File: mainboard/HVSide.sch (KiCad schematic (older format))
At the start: 50 parts, among them J11 CONN_2X2, J17 HV, J18 CONN_1X2, J19 CONN_1X2, J4 CONN_2X2, U10 DCDC_ISO_5V_ISO, U15 CD4082, U16 ADCMP350, U19 TCMT1103, U23 CD4072BPW, U24 LM358, U26 TCMT1103, U27 DCDC_ISO_5V, U28 MIC5365-3.3YC5, U29 Si8900, U30 MAX14878AWA+, U7 ADCMP354

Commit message: Added 64pin mcu and moved isocanspi to HV sheet
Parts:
- added C? (x3): 100nF, Capacitor_SMD:C_0603_1608Metric, symbol Device:C_Small
- added R?: 330K, Resistor_SMD:R_0603_1608Metric, symbol Device:R
- added R?: 604, Resistor_SMD:R_0603_1608Metric, symbol Device:R
- added R?: 1K4, Resistor_SMD:R_0603_1608Metric, symbol Device:R
- added R? (x2): 150, Resistor_SMD:R_0603_1608Metric, symbol Device:R
- added R?: 120, Resistor_SMD:R_0805_2012Metric, symbol Device:R
- added U?: HM2103, MainBoard:HM2103, symbol MainBoard:HM2103
- added U?: LTC6820, MainBoard:MSOP-16, symbol MainBoard:LTC6820
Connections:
- net +3V3: now also C?.1, R?.1, U?.6 (VDDs)
- net +5V: now also C?.1, U?.12 (MSTR), U?.9 (VDD)
- net GND: now also C?.1, C?.2, C?.2, R?.1, U?.1 (EN), U?.13 (SLOW), U?.14 (GND), U?.7 (POL), U?.8 (PHA)
- net ISO_CANH renamed ISO_CANH_IP
- net ISO_CANH_IP: now also J11.1 (Pin_1), R?.2, U?.3; no longer J11.2 (Pin_2)
- net ISO_CANL renamed ISO_CANL_IM
- net ISO_CANL_IM: now also J11.2 (Pin_2), R?.1, U?.1; no longer J11.1 (Pin_1)
- new net: C?.2, R?.1, R?.2
- new net CS_6820: U?.5 (~CS)
- new net IBIAS: R?.2, U?.16 (IBIAS)
- new net ICMP: R?.1, R?.2, U?.15 (ICMP)
- new net IM_LV: R?.2, U?.10 (IM), U?.6
- new net IP_LV: R?.1, U?.11 (IP), U?.4
- new net MOSI: U?.2 (MOSI)
- new net SCK: U?.4 (SCK)
- no-connect marks 6 -> 8
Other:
- note added: "ISOLATED PACK VOLTAGE ADC via UART"
- note added: "ISOLATED VOLTAGE SUPPLIES"
- note added: "PRECHARGE_STATUS = TS_exceed_60Vdc & PRECHARGE_ON\n"
- note added: "PROMINENT INDICATOR"
- note added: "choose only one between up or down circuits"
- note added: "isoCAN INTERFACE"
- note added: "isoCAN/SPI"
- note added: "isoSPI INTERFACE"
- note added: "isolation"
- note removed: "CAN_ISO"
- note removed: "ISOLATED VOLTAGE SOURCES"
- note removed: "PRECHARGE_STATUS = TS_exceed_60Vdc && PRECHARGE_ON\n"
- note removed: "PROMINENT INDICTOR"
- note removed: "UART ISOLATED PACK VOLTAGE ADC"
- moved on the sheet: C16, C17, C27, J11, J17, J18, J19, J4, R59, U10, U16, U30

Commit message: added the stm32 configuration, neaten schematic
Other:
- note added: "HV"
- note added: "LV"
- moved on the sheet: C16, C17, C26, C27, C40, C41, C43, C?, D4, J11, J17, J18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

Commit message: general changes and comments, still WIP
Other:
- note added: "Isolated power supply to power the \nHV-side elements from the BMS-side 5V"
- note added: "Prominent\nIndicator\n25mA"
- note added: "Supply from the first cell to be \nsure the prominent is powered.\nONLY CONNECT THE FIRST CELL\n BECAUSE OF BOARD CLEARANCES"
- note removed: "Prominent\nIndicator"
- moved on the sheet: C17, U10
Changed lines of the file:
@@
 Wire Wire Line
 	1050 3100 950  3100
-Text Notes 4650 1000 2    50   ~ 0
-Prominent\nIndicator
+Text Notes 4250 1000 0    50   ~ 0
+Prominent\nIndicator\n25mA
 Wire Wire Line
 	7000 4100 7250 4100
@@
 Text HLabel 8200 1100 2    50   Input ~ 0
 si890x_reset
-Text Label 1950 1300 0    50   ~ 0
+Text Label 1950 1150 0    50   ~ 0
 5V_FROM_CELL
 $Comp
 L Device:C C17
 U 1 1 5E5BFB93
-P 2350 1450
-F 0 "C17" H 2465 1496 50  0000 L CNN
-F 1 "1uF" H 2465 1405 50  0000 L CNN
-F 2 "Capacitor_SMD:C_0805_2012Metric" H 2388 1300 50  0001 C CNN
-F 3 "https://www.mouser.it/ProductDetail/AVX/12102C105KAZ2A?qs=sGAEpiMZZMs0AnBnWHyRQN7%2FAA2D2lPPDCdjTtfSValCgVFFyRxU%2FQ%3D%3D" H 2350 1450 50  0001 C CNN
-	1    2350 1450
+P 2350 1300
+F 0 "C17" H 2465 1346 50  0000 L CNN
+F 1 "1uF" H 2465 1255 50  0000 L CNN
+F 2 "Capacitor_SMD:C_0805_2012Metric" H 2388 1150 50  0001 C CNN
+F 3 "https://www.mouser.it/ProductDetail/AVX/12102C105KAZ2A?qs=sGAEpiMZZMs0AnBnWHyRQN7%2FAA2D2lPPDCdjTtfSValCgVFFyRxU%2FQ%3D%3D" H 2350 1300 50  0001 C CNN
+	1    2350 1300
 	1    0    0    -1
 $EndComp
@@
 L power:-BATT #PWR0104
 U 1 1 5E5C001A
-P 2350 1600
-F 0 "#PWR0104" H 2350 1450 50  0001 C CNN
-F 1 "-BATT" H 2350 1750 50  0000 C CNN
-F 2 "" H 2350 1600 50  0001 C CNN
-F 3 "" H 2350 1600 50  0001 C CNN
-	1    2350 1600
-	-1   0    0    1
-$EndComp
-Wire Wire Line
-	1950 1300 2350 1300
+P 2350 1450
+F 0 "#PWR0104" H 2350 1300 50  0001 C CNN
+F 1 "-BATT" H 2350 1600 50  0000 C CNN
+F 2 "" H 2350 1450 50  0001 C CNN
+F 3 "" H 2350 1450 50  0001 C CNN
+	1    2350 1450
+	-1   0    0    1
+$EndComp
+Wire Wire Line
+	1950 1150 2350 1150
 $Comp
 L Device:C C26
@@
 L MainBoard:DCDC_ISO_12V_ISO U10
 U 1 1 5E5FCD5F
-P 1500 1300
-F 0 "U10" H 1525 1565 50  0000 C CNN
-F 1 "DCDC_ISO_5V_ISO" H 1525 1474 50  0000 C CNN
-F 2 "MainBoard:DC_DC_ISO_ROExxxx" H 1500 1300 50  0001 C CNN
-F 3 "" H 1500 1300 50  0001 C CNN
-	1    1500 1300
+P 1500 1150
+F 0 "U10" H 1525 1415 50  0000 C CNN
+F 1 "DCDC_ISO_5V_ISO" H 1525 1324 50  0000 C CNN
+F 2 "MainBoard:DC_DC_ISO_ROExxxx" H 1500 1150 50  0001 C CNN
+F 3 "" H 1500 1150 50  0001 C CNN
+	1    1500 1150
 	1    0    0    -1
 $EndComp
@@
 L power:-BATT #PWR0106
 U 1 1 5E616F05
-P 1950 1450
-F 0 "#PWR0106" H 1950 1300 50  0001 C CNN
-F 1 "-BATT" H 1950 1600 50  0000 C CNN
-F 2 "" H 1950 1450 50  0001 C CNN
-F 3 "" H 1950 1450 50  0001 C CNN
-	1    1950 1450
+P 1950 1300
+F 0 "#PWR0106" H 1950 1150 50  0001 C CNN
+F 1 "-BATT" H 1950 1450 50  0000 C CNN
+F 2 "" H 1950 1300 50  0001 C CNN
+F 3 "" H 1950 1300 50  0001 C CNN
+	1    1950 1300
 	1    0    0    1
 $EndComp
@@
 Text Notes 5800 1300 0    50   ~ 0
 IMD_TS+
-Text Notes 1050 950  0    50   ~ 0
+Text Notes 1900 550  0    50   ~ 0
 EXT_POWER&PROMIMENT
 Text Notes 4650 5200 0    50   ~ 0
@@
 Text Label 2300 800  2    50   ~ 0
 EXT_5V
-Text Label 650  1450 0    50   ~ 0
+Text Label 650  1300 0    50   ~ 0
 EXT_GND
 Wire Wire Line
-	1100 1300 650  1300
-Text Label 650  1300 0    50   ~ 0
+	1100 1150 650  1150
+Text Label 650  1150 0    50   ~ 0
 EXT_5V
 Wire Wire Line
-	650  1450 1100 1450
+	650  1300 1100 1300
 Wire Notes Line
 	4150 650  4150 1200
@@
 Text Notes 4050 7750 1    50   Italic 0
 LV
+Text Notes 550  1750 0    50   ~ 0
+Supply from the first cell to be \nsure the prominent is powered.\nONLY CONNECT THE FIRST CELL\n BECAUSE OF BOARD CLEARANCES
+Text Notes 6950 3300 0    50   ~ 0
+Isolated power supply to power the \nHV-side elements from the BMS-side 5V
 $EndSCHEMATC

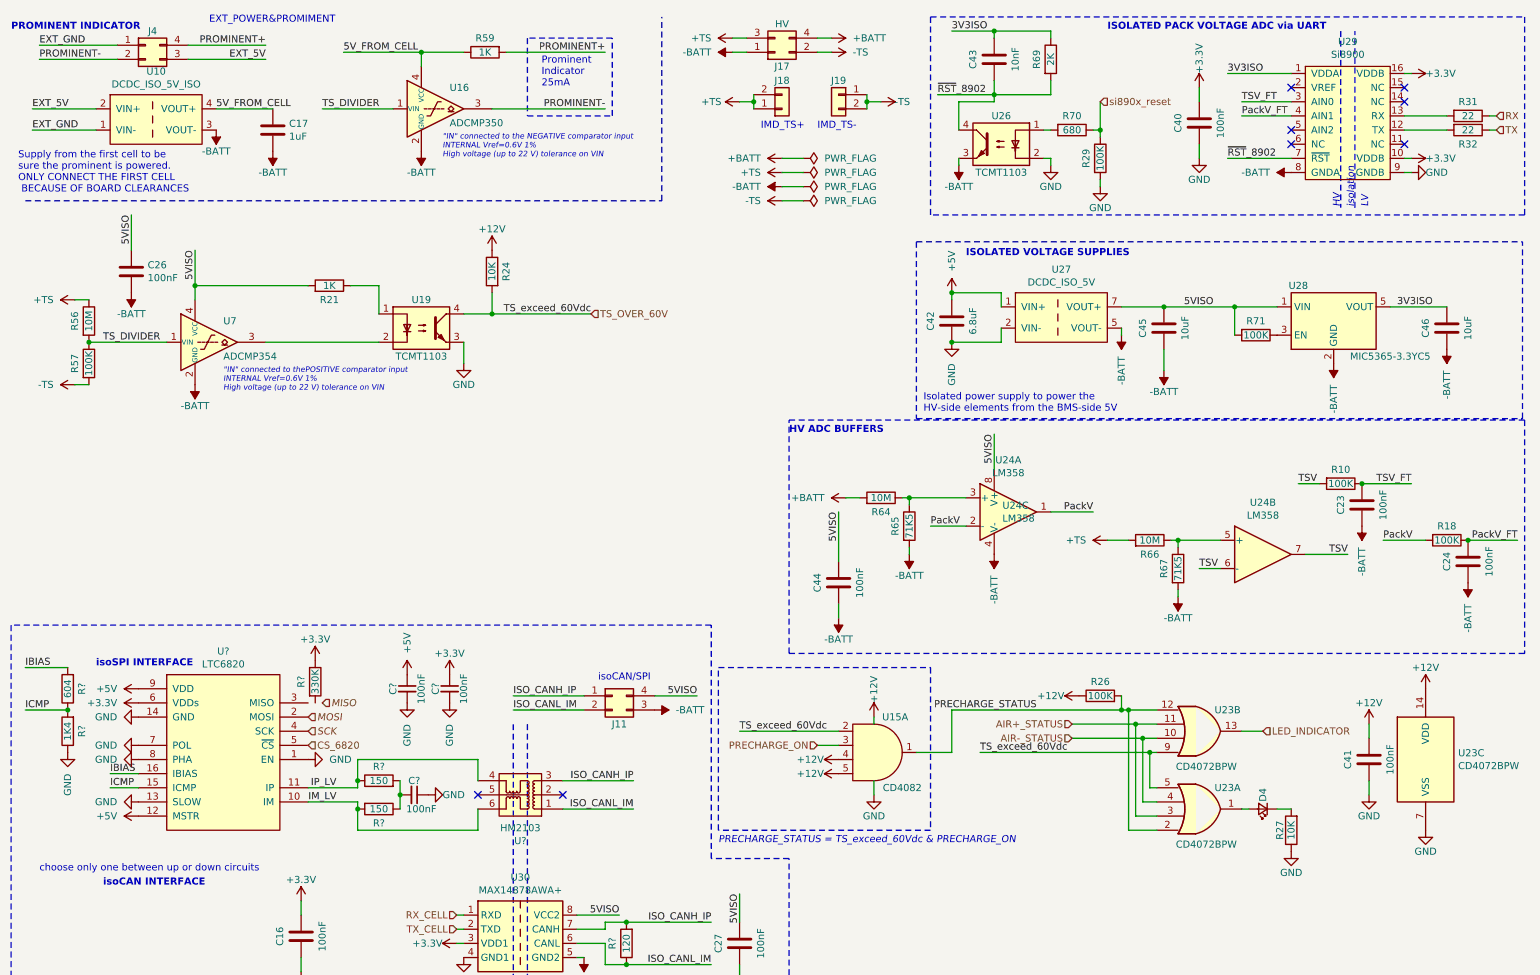
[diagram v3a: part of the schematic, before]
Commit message: 64pin, testpoints, commenting, general refactoring
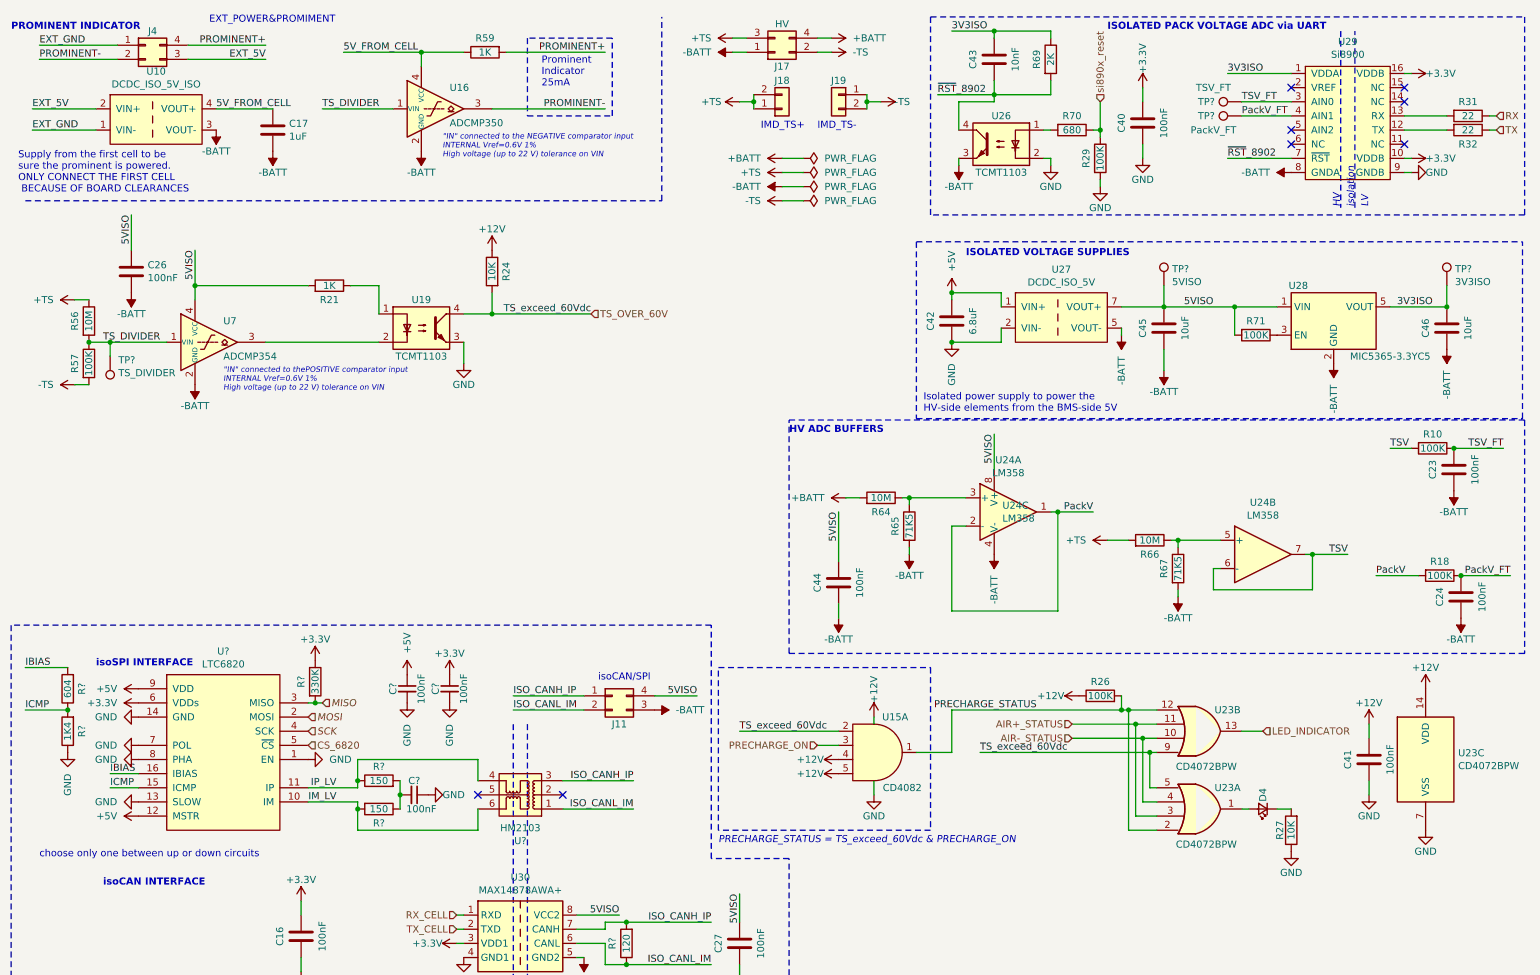
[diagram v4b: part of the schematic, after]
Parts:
- added TP?: TS_DIVIDER, symbol Connector:TestPoint
- added TP?: 5VISO, symbol Connector:TestPoint
- added TP?: 3V3ISO, symbol Connector:TestPoint
- added TP?: TSV_FT, symbol Connector:TestPoint
- added TP?: PackV_FT, symbol Connector:TestPoint
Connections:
- net 3V3ISO: now also TP?.1
- net 5VISO: now also TP?.1
- net MISO: now also R?.2, U?.3 (MISO)
- net PackV_FT: now also TP?.1
- net TSV_FT: now also TP?.1
- net TS_DIVIDER: now also TP?.1
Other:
- moved on the sheet: C23, C24, C40, R10, R18
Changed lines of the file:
@@
 Text Notes 4250 1000 0    50   ~ 0
 Prominent\nIndicator\n25mA
-Wire Wire Line
-	7000 4100 7250 4100
 Text Notes 6000 3450 0    50   ~ 10
 HV ADC BUFFERS
@@
 	-1   0    0    1
 $EndComp
-Text Label 7000 4100 0    50   ~ 0
-PackV
 Wire Wire Line
 	8350 2750 8350 2700
@@
 	6850 3900 6850 3950
 Wire Wire Line
-	8150 4000 7850 4000
+	8150 4000 7900 4000
 Text Label 8150 4000 2    50   ~ 0
 PackV
@@
 L Device:C C40
 U 1 1 5DED2D06
-P 8900 1250
-F 0 "C40" V 8750 1250 50  0000 C CNN
-F 1 "100nF" V 9050 1250 50  0000 C CNN
-F 2 "Capacitor_SMD:C_0603_1608Metric" H 8938 1100 50  0001 C CNN
-F 3 "~" H 8900 1250 50  0001 C CNN
-	1    8900 1250
-	1    0    0    -1
-$EndComp
-Wire Wire Line
-	8900 1000 8900 1100
-Wire Wire Line
-	8900 1400 8900 1500
+P 8500 1250
+F 0 "C40" V 8350 1250 50  0000 C CNN
+F 1 "100nF" V 8650 1250 50  0000 C CNN
+F 2 "Capacitor_SMD:C_0603_1608Metric" H 8538 1100 50  0001 C CNN
+F 3 "~" H 8500 1250 50  0001 C CNN
+	1    8500 1250
+	1    0    0    -1
+$EndComp
+Wire Wire Line
+	8500 1000 8500 1100
+Wire Wire Line
+	8500 1400 8500 1500
 $Comp
 L power:+3.3V #PWR?
 U 1 1 5DEDABF8
-P 8900 1000
+P 8500 1000
 AR Path="/5DEDABF8" Ref="#PWR?"  Part="1"
 AR Path="/5B50ED38/5DEDABF8" Ref="#PWR0203"  Part="1"
-F 0 "#PWR0203" H 8900 850 50  0001 C CNN
-F 1 "+3.3V" V 8900 1100 50  0000 L CNN
-F 2 "" H 8900 1000 50  0001 C CNN
-F 3 "" H 8900 1000 50  0001 C CNN
-	1    8900 1000
+F 0 "#PWR0203" H 8500 850 50  0001 C CNN
+F 1 "+3.3V" V 8500 1100 50  0000 L CNN
+F 2 "" H 8500 1000 50  0001 C CNN
+F 3 "" H 8500 1000 50  0001 C CNN
+	1    8500 1000
 	1    0    0    -1
 $EndComp
@@
 L Device:C C23
 U 1 1 5E610DCE
-P 10050 3950
-F 0 "C23" V 9900 3950 50  0000 C CNN
-F 1 "100nF" V 10200 3950 50  0000 C CNN
-F 2 "Capacitor_SMD:C_0603_1608Metric" H 10088 3800 50  0001 C CNN
-F 3 "~" H 10050 3950 50  0001 C CNN
-	1    10050 3950
+P 10700 3700
+F 0 "C23" V 10550 3700 50  0000 C CNN
+F 1 "100nF" V 10850 3700 50  0000 C CNN
+F 2 "Capacitor_SMD:C_0603_1608Metric" H 10738 3550 50  0001 C CNN
+F 3 "~" H 10700 3700 50  0001 C CNN
+	1    10700 3700
 	1    0    0    -1
 $EndComp
@@
 	1    0    0    -1
 $EndComp
-Text Label 8900 4400 0    50   ~ 0
-TSV
-Wire Wire Line
-	9050 4400 8900 4400
+Wire Wire Line
+	9050 4400 9000 4400
 Text Label 9950 4300 2    50   ~ 0
 TSV
 Wire Wire Line
-	9650 4300 9950 4300
+	9650 4300 9700 4300
 Wire Wire Line
 	8700 4200 8750 4200
@@
 Wire Wire Line
 	8750 4600 8750 4550
-Text Label 9600 3800 0    50   ~ 0
+Text Label 10250 3550 0    50   ~ 0
 TSV
 Wire Wire Line
-	9600 3800 9750 3800
+	10250 3550 10400 3550
 $Comp
 L Device:R R10
 U 1 1 5E6349F0
-P 9900 3800
-F 0 "R10" V 9800 3800 50  0000 C CNN
-F 1 "100K" V 9900 3800 50  0000 C CNN
-F 2 "Resistor_SMD:R_0603_1608Metric" V 9830 3800 50  0001 C CNN
-F 3 "~" H 9900 3800 50  0001 C CNN
-	1    9900 3800
+P 10550 3550
+F 0 "R10" V 10450 3550 50  0000 C CNN
+F 1 "100K" V 10550 3550 50  0000 C CNN
+F 2 "Resistor_SMD:R_0603_1608Metric" V 10480 3550 50  0001 C CNN
+F 3 "~" H 10550 3550 50  0001 C CNN
+	1    10550 3550
 	0    1    1    0
 $EndComp
@@
 L power:-BATT #PWR0188
 U 1 1 5E653F92
-P 10050 4100
-F 0 "#PWR0188" H 10050 3950 50  0001 C CNN
-F 1 "-BATT" V 10050 4250 50  0000 L CNN
-F 2 "" H 10050 4100 50  0001 C CNN
-F 3 "" H 10050 4100 50  0001 C CNN
-	1    10050 4100
+P 10700 3850
+F 0 "#PWR0188" H 10700 3700 50  0001 C CNN
+F 1 "-BATT" H 10600 4000 50  0000 L CNN
+F 2 "" H 10700 3850 50  0001 C CNN
+F 3 "" H 10700 3850 50  0001 C CNN
+	1    10700 3850
 	-1   0    0    1
 $EndComp
@@
 L Device:C C24
 U 1 1 5E654C1C
-P 10800 4350
-F 0 "C24" V 10650 4350 50  0000 C CNN
-F 1 "100nF" V 10950 4350 50  0000 C CNN
-F 2 "Capacitor_SMD:C_0603_1608Metric" H 10838 4200 50  0001 C CNN
-F 3 "~" H 10800 4350 50  0001 C CNN
-	1    10800 4350
-	1    0    0    -1
-$EndComp
-Wire Wire Line
-	10200 4200 10500 4200
+P 10750 4600
+F 0 "C24" V 10600 4600 50  0000 C CNN
+F 1 "100nF" V 10900 4600 50  0000 C CNN
+F 2 "Capacitor_SMD:C_0603_1608Metric" H 10788 4450 50  0001 C CNN
+F 3 "~" H 10750 4600 50  0001 C CNN
+	1    10750 4600
+	1    0    0    -1
+$EndComp
+Wire Wire Line
+	10150 4450 10450 4450
 $Comp
 L Device:R R18
 U 1 1 5E654C24
-P 10650 4200
-F 0 "R18" V 10550 4200 50  0000 C CNN
-F 1 "100K" V 10650 4200 50  0000 C CNN
-F 2 "Resistor_SMD:R_0603_1608Metric" V 10580 4200 50  0001 C CNN
-F 3 "~" H 10650 4200 50  0001 C CNN
-	1    10650 4200
+P 10600 4450
+F 0 "R18" V 10500 4450 50  0000 C CNN
+F 1 "100K" V 10600 4450 50  0000 C CNN
+F 2 "Resistor_SMD:R_0603_1608Metric" V 10530 4450 50  0001 C CNN
+F 3 "~" H 10600 4450 50  0001 C CNN
+	1    10600 4450
 	0    1    1    0
 $EndComp
@@
 L power:-BATT #PWR0191
 U 1 1 5E654C2A
-P 10800 4500
-F 0 "#PWR0191" H 10800 4350 50  0001 C CNN
-F 1 "-BATT" V 10800 4650 50  0000 L CNN
-F 2 "" H 10800 4500 50  0001 C CNN
-F 3 "" H 10800 4500 50  0001 C CNN
-	1    10800 4500
-	-1   0    0    1
-$EndComp
-Text Label 10200 4200 0    50   ~ 0
+P 10750 4750
+F 0 "#PWR0191" H 10750 4600 50  0001 C CNN
+F 1 "-BATT" H 10650 4900 50  0000 L CNN
+F 2 "" H 10750 4750 50  0001 C CNN
+F 3 "" H 10750 4750 50  0001 C CNN
+	1    10750 4750
+	-1   0    0    1
+$EndComp
+Text Label 10150 4450 0    50   ~ 0
 PackV
 Wire Wire Line
-	10050 3800 10400 3800
-Connection ~ 10050 3800
-Text Label 10400 3800 2    50   ~ 0
+	10700 3550 11050 3550
+Connection ~ 10700 3550
+Text Label 11050 3550 2    50   ~ 0
 TSV_FT
-Text Label 11150 4200 2    50   ~ 0
+Text Label 11100 4450 2    50   ~ 0
 PackV_FT
 Wire Wire Line
-	11150 4200 10800 4200
-Connection ~ 10800 4200
+	11100 4450 10750 4450
+Connection ~ 10750 4450
 $Comp
 L Device:C C46
@@
 	1    0    0    -1
 $EndComp
-Text HLabel 8200 1100 2    50   Input ~ 0
+Text HLabel 8200 1100 1    50   Input ~ 0
 si890x_reset
 Text Label 1950 1150 0    50   ~ 0
@@
 	3400 850  3400 750
 Wire Wire Line
-	1050 2800 1600 2800
+	1050 2800 1200 2800
 Text Label 1150 2800 0    50   ~ 0
 TS_DIVIDER
@@
 L power:GND #PWR?
 U 1 1 5F74B6B4
-P 8900 1500
+P 8500 1500
 AR Path="/5B045B0D/5F74B6B4" Ref="#PWR?"  Part="1"
 AR Path="/5B50ED38/5F74B6B4" Ref="#PWR0204"  Part="1"
-F 0 "#PWR0204" H 8900 1250 50  0001 C CNN
-F 1 "GND" H 8900 1350 50  0000 C CNN
-F 2 "" H 8900 1500 50  0001 C CNN
-F 3 "" H 8900 1500 50  0001 C CNN
-	1    8900 1500
+F 0 "#PWR0204" H 8500 1250 50  0001 C CNN
+F 1 "GND" H 8500 1350 50  0000 C CNN
+F 2 "" H 8500 1500 50  0001 C CNN
+F 3 "" H 8500 1500 50  0001 C CNN
+	1    8500 1500
 	1    0    0    -1
 $EndComp
@@
 Text Notes 1150 6650 0    50   ~ 10
 isoCAN INTERFACE
-Text Notes 700  6550 0    50   ~ 0
+Text Notes 700  6450 0    50   ~ 0
 choose only one between up or down circuits
 $Comp
@@
 Text Notes 6950 3300 0    50   ~ 0
 Isolated power supply to power the \nHV-side elements from the BMS-side 5V
+$Comp
+L Connector:TestPoint TP?
+U 1 1 606342E3
+P 1200 2900
+F 0 "TP?" H 1142 2926 50  0000 R CNN
+F 1 "TS_DIVIDER" H 1142 3017 50  0000 R CNN
+F 2 "" H 1400 2900 50  0001 C CNN
+F 3 "~" H 1400 2900 50  0001 C CNN
+	1    1200 2900
+	-1   0    0    1
+$EndComp
+Connection ~ 1200 2800
+Wire Wire Line
+	1200 2800 1600 2800
+Wire Wire Line
+	1200 2800 1200 2900
+$Comp
+L Connector:TestPoint TP?
+U 1 1 60640919
+P 8650 2400
+F 0 "TP?" H 8708 2518 50  0000 L CNN
+F 1 "5VISO" H 8708 2427 50  0000 L CNN
+F 2 "" H 8850 2400 50  0001 C CNN
+F 3 "~" H 8850 2400 50  0001 C CNN
+	1    8650 2400
+	1    0    0    -1
+$EndComp
+$Comp
+L Connector:TestPoint TP?
+U 1 1 60640DAD
+P 10650 2400
+F 0 "TP?" H 10708 2518 50  0000 L CNN
+F 1 "3V3ISO" H 10708 2427 50  0000 L CNN
+F 2 "" H 10850 2400 50  0001 C CNN
+F 3 "~" H 10850 2400 50  0001 C CNN
+	1    10650 2400
+	1    0    0    -1
+$EndComp
+Wire Wire Line
+	10650 2400 10650 2550
+Connection ~ 10650 2550
+Wire Wire Line
+	8650 2400 8650 2550
+$Comp
+L Connector:TestPoint TP?
+U 1 1 60660D04
+P 9200 1100
+F 0 "TP?" V 9200 1350 50  0000 C CNN
+F 1 "TSV_FT" V 9300 1300 50  0000 C CNN
+F 2 "" H 9400 1100 50  0001 C CNN
+F 3 "~" H 9400 1100 50  0001 C CNN
+	1    9200 1100
+	0    -1   -1   0
+$EndComp
+$Comp
+L Connector:TestPoint TP?
+U 1 1 60661782
+P 9200 1200
+F 0 "TP?" V 9200 1450 50  0000 C CNN
+F 1 "PackV_FT" V 9100 1400 50  0000 C CNN
+F 2 "" H 9400 1200 50  0001 C CNN
+F 3 "~" H 9400 1200 50  0001 C CNN
+	1    9200 1200
+	0    -1   -1   0
+$EndComp
+Wire Wire Line
+	7900 4000 7900 4700
+Wire Wire Line
+	7900 4700 7150 4700
+Wire Wire Line
+	7150 4700 7150 4100
+Connection ~ 7900 4000
+Wire Wire Line
+	7900 4000 7850 4000
+Wire Wire Line
+	7150 4100 7250 4100
+Wire Wire Line
+	9700 4300 9700 4550
+Wire Wire Line
+	9700 4550 9000 4550
+Wire Wire Line
+	9000 4550 9000 4400
+Connection ~ 9700 4300
+Wire Wire Line
+	9700 4300 9950 4300
+Wire Wire Line
+	2600 5350 2650 5350
+Connection ~ 2650 5350
+Wire Wire Line
+	2650 5350 2700 5350
 $EndSCHEMATC
